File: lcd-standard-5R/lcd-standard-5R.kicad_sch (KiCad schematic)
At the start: 109 parts, among them J1 SWD, J2 Conn_01x40_MountingPin, J3 Micro_SD_Card_Det1, J5 Conn_01x06_MountingPin, J6 Serial, J7 Conn_ARM_JTAG_SWD_10, J8 Conn_01x02_MountingPin, J9 Conn_01x10_MountingPin, Q1 DMG2301L, Q2 MMBT3904, Q3 MMBT3904, Q4 MMBT3904, SW1 BOOT0, SW2 RST, U1 MAX98357A, U2 TPS61169, U3 XPT2046TS, U4 CAT24C256, U5 AMS1117-3.3, U6 siplex-som-s16

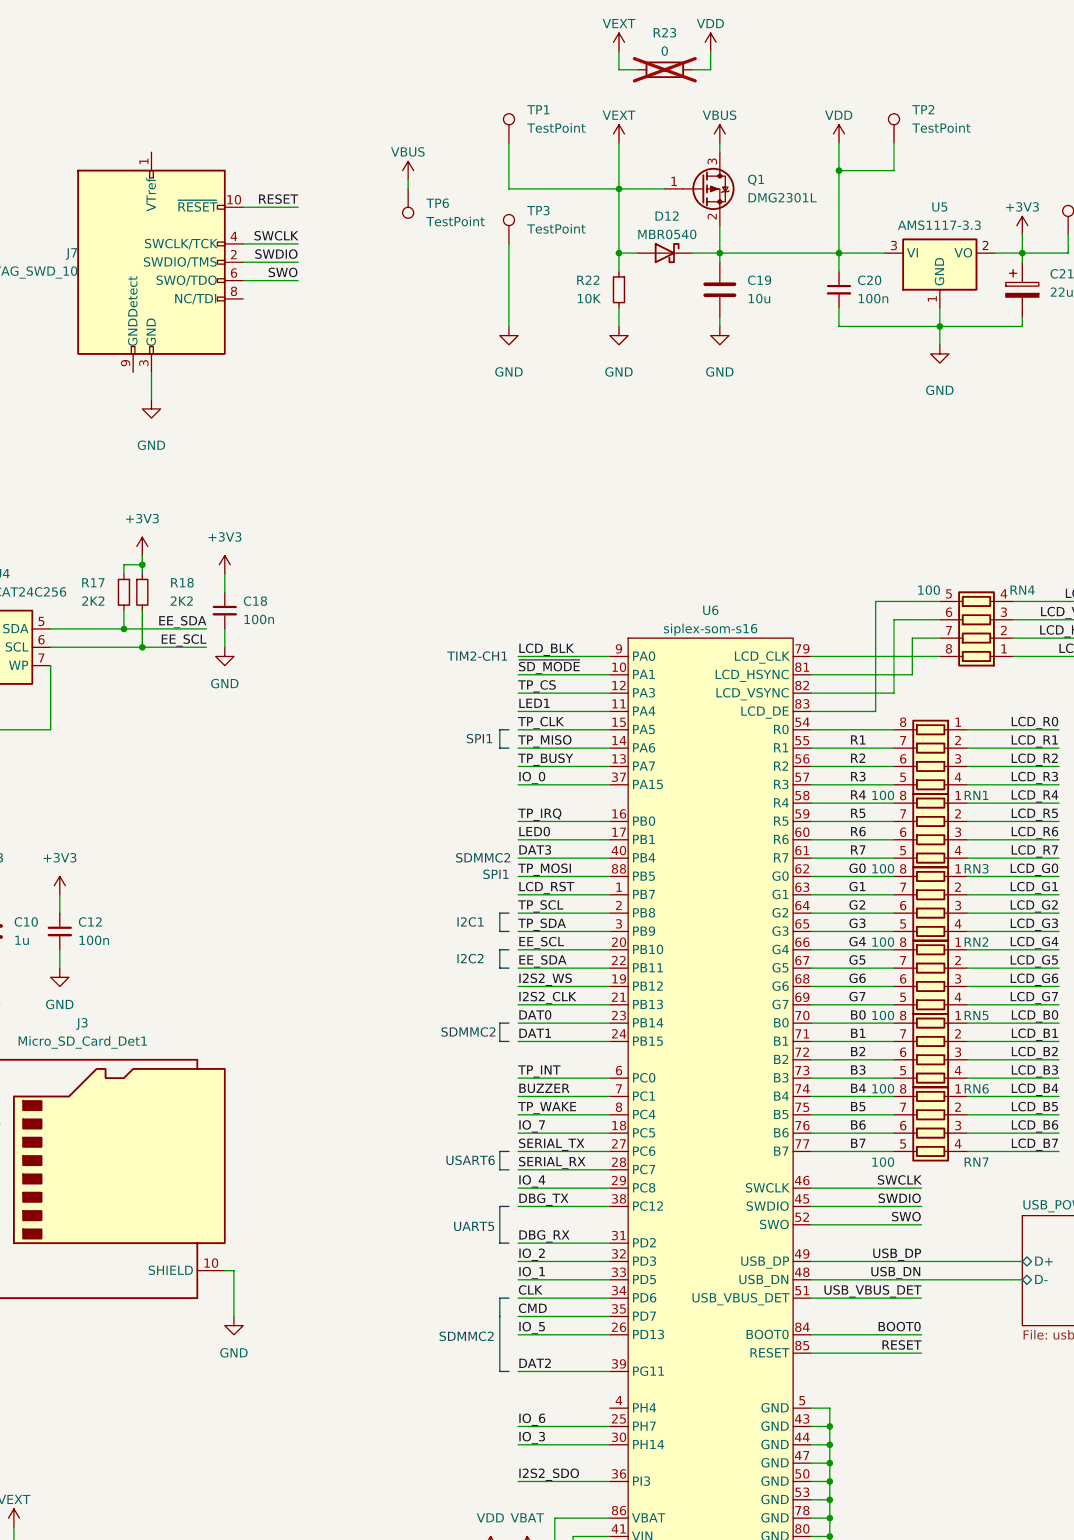
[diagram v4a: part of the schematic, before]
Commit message: Added sd_det tracks
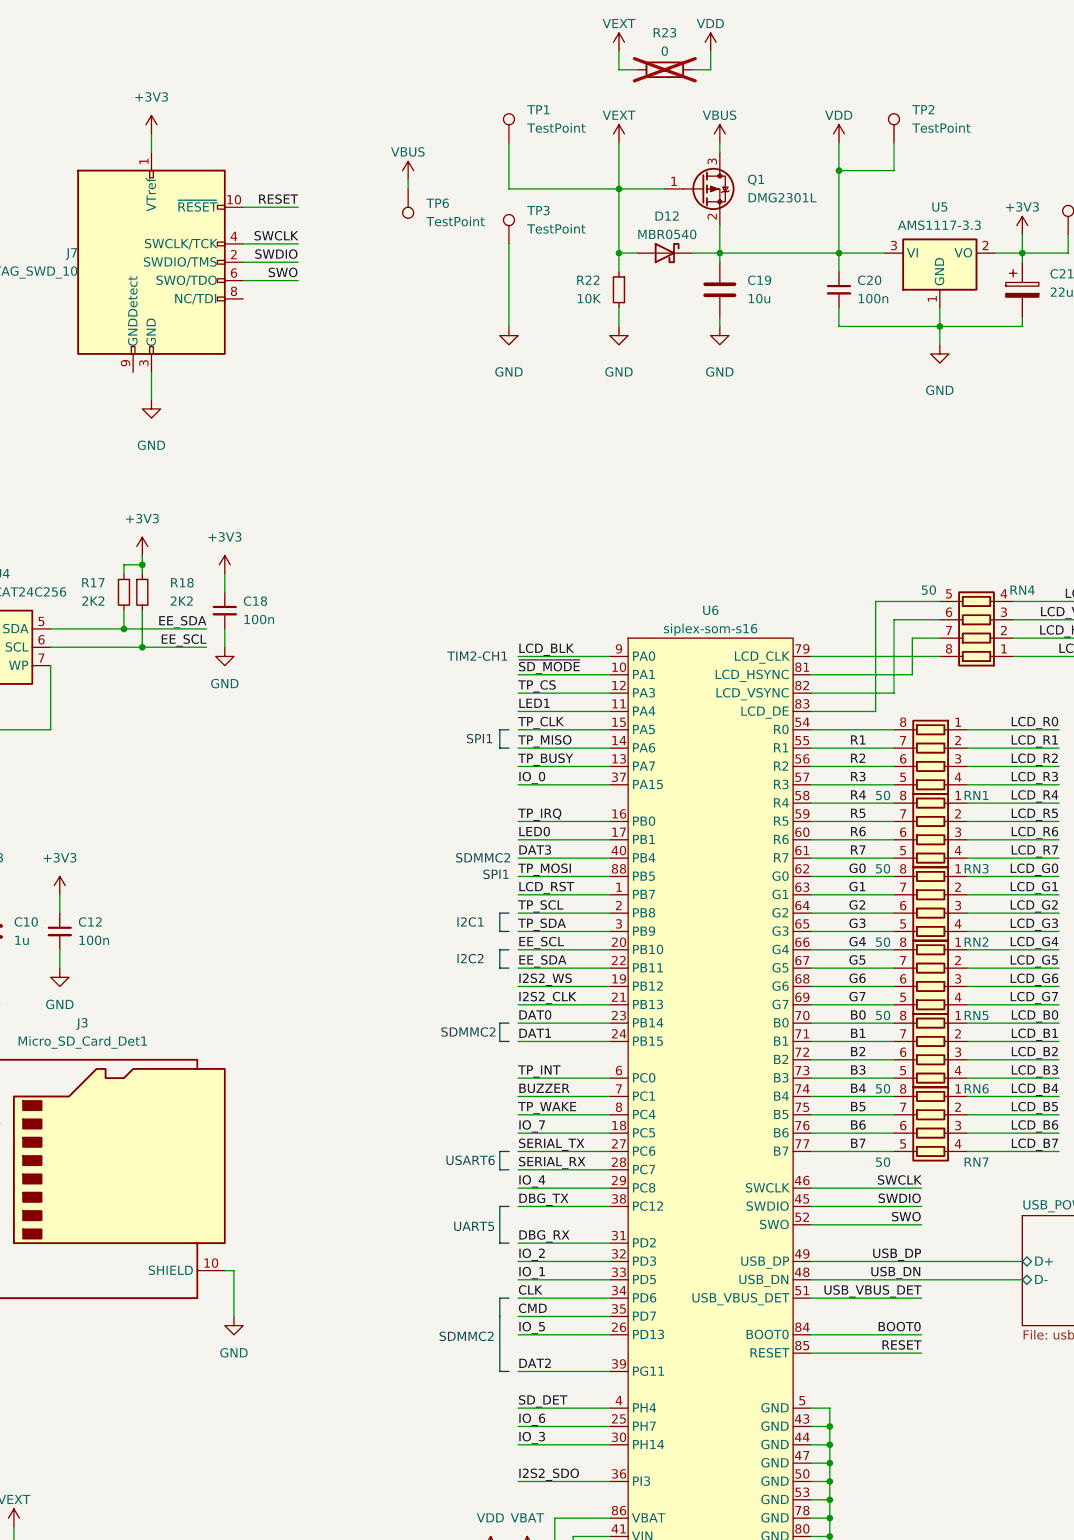
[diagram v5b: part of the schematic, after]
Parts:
- J5: footprint Connector_FFC-FPC:Hirose_FH12-6S-0.5SH_1x06-1MP_P0.50mm_Horizontal -> Connector_FPC:Conn_FPC_6P_0.5mm_XUNPU_FPC-05FB-6PH20
- J9: footprint Connector_JST:JST_SHL_SM10B-SHLS-TF_1x10-1MP_P1.00mm_Horizontal -> Connector_FPC:Conn_FPC_10P_1mm_G-SWITCH_GT-F1008SR20-10SMT01
- RN1, RN2, RN3, RN4, RN5, RN6, RN7: value 100 -> 50
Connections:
- net +3V3: now also J7.1 (VTref)
- net SD_DET: now also U6.4 (PH4)
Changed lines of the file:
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@@
 	(wire
 		(pts
+			(xy -26.67 -38.1) (xy -26.67 -35.56)
+		)
+		(stroke
+			(width 0)
+			(type default)
+		)
+	)
+	(wire
+		(pts
 			(xy 99.06 82.55) (xy 86.36 82.55)
 		)
@@
 	(wire
 		(pts
+			(xy 24.13 138.43) (xy 36.83 138.43)
+		)
+		(stroke
+			(width 0)
+			(type default)
+		)
+	)
+	(wire
+		(pts
 			(xy 238.76 64.77) (xy 251.46 64.77)
 		)
@@
 		)
 	)
+	(label "SD_DET"
+		(at 24.13 138.43 0)
+		(fields_autoplaced yes)
+		(effects
+			(font
+				(size 1.27 1.27)
+			)
+			(justify left bottom)
+		)
+	)
 	(label "SERIAL_TX"
 		(at 24.13 102.87 0)
@@
 			)
 		)
-		(property "Value" "100"
+		(property "Value" "50"
 			(at 74.676 53.594 90)
 			(effects
@@
 			)
 		)
-		(property "Value" "100"
+		(property "Value" "50"
 			(at 74.676 73.914 90)
 			(effects
@@
 			)
 		)
-		(property "Footprint" "Connector_FFC-FPC:Hirose_FH12-6S-0.5SH_1x06-1MP_P0.50mm_Horizontal"
+		(property "Footprint" "Connector_FPC:Conn_FPC_6P_0.5mm_XUNPU_FPC-05FB-6PH20"
 			(at 342.9 180.34 0)
 			(effects
@@
 	)
 	(symbol
+		(lib_id "power:+3V3")
+		(at -26.67 -38.1 0)
+		(unit 1)
+		(exclude_from_sim no)
+		(in_bom yes)
+		(on_board yes)
+		(dnp no)
+		(fields_autoplaced yes)
+		(property "Reference" "#PWR0107"
+			(at -26.67 -34.29 0)
+			(effects
+				(font
+					(size 1.27 1.27)
+				)
+				(hide yes)
+			)
+		)
+		(property "Value" "+3V3"
+			(at -26.67 -43.18 0)
+			(effects
+				(font
+					(size 1.27 1.27)
+				)
+			)
+		)
+		(property "Footprint" ""
+			(at -26.67 -38.1 0)
+			(effects
+				(font
+					(size 1.27 1.27)
+				)
+				(hide yes)
+			)
+		)
+		(property "Datasheet" ""
+			(at -26.67 -38.1 0)
+			(effects
+				(font
+					(size 1.27 1.27)
+				)
+				(hide yes)
+			)
+		)
+		(property "Description" "Power symbol creates a global label with name \"+3V3\""
+			(at -26.67 -38.1 0)
+			(effects
+				(font
+					(size 1.27 1.27)
+				)
+				(hide yes)
+			)
+		)
+		(pin "1"
+		)
+		(instances
+			(project "lcd-standard-5R"
+				(path "/a9fe5be7-3a80-455e-a721-d53819db4a52"
+					(reference "#PWR0107")
+					(unit 1)
+				)
+			)
+		)
+	)
+	(symbol
 		(lib_id "Device:C_Polarized")
 		(at 93.98 -16.51 0)
@@
 			)
 		)
-		(property "Value" "100"
+		(property "Value" "50"
 			(at 74.676 94.234 90)
 			(effects
@@
 			)
 		)
-		(property "Value" "100"
+		(property "Value" "50"
 			(at 74.676 104.394 90)
 			(effects
@@
 			)
 		)
-		(property "Value" "100"
+		(property "Value" "50"
 			(at 74.676 63.754 90)
 			(effects
@@
 			)
 		)
-		(property "Value" "100"
+		(property "Value" "50"
 			(at 74.676 84.074 90)
 			(effects
@@
 			)
 		)
-		(property "Footprint" "Connector_JST:JST_SHL_SM10B-SHLS-TF_1x10-1MP_P1.00mm_Horizontal"
+		(property "Footprint" "Connector_FPC:Conn_FPC_10P_1mm_G-SWITCH_GT-F1008SR20-10SMT01"
 			(at -107.95 49.53 0)
 			(effects
@@
 			)
 		)
-		(property "Value" "100"
+		(property "Value" "50"
 			(at 81.026 25.146 90)
 			(effects

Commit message: Slight changes
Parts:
- BT2: JLCPCB Part # (none) -> C70381
- BZ1: JLCPCB Part # (none) -> C255327
- C1: value 10u -> 10u/1206; JLCPCB Part # (none) -> C13585
- C10, C2, C22, C3: JLCPCB Part # (none) -> C15849
- C11, C19, C5, C7: JLCPCB Part # (none) -> C15850
- C12, C18: JLCPCB Part # (none) -> C1525
- C13, C14, C15, C16, C17, C20, C23, C4, C6: footprint Capacitor_SMD:C_0603_1608Metric -> Capacitor_SMD:C_0402_1005Metric; JLCPCB Part # (none) -> C1525
- C21: value 22uF -> 10uF; footprint Capacitor_Tantalum_SMD:CP_EIA-3528-12_Kemet-T -> Capacitor_Tantalum_SMD:CP_EIA-3216-18_Kemet-A; JLCPCB Part # (none) -> C7171
- D1: value NSR0320MW2T1G -> B5819WS; JLCPCB Part # (none) -> C64886
- D10, D11: JLCPCB Part # (none) -> C47546
- D12: value MBR0540 -> B5819W; JLCPCB Part # (none) -> C7420330
- D2: JLCPCB Part # (none) -> C7420330
- D3, D4: value LED -> RED; JLCPCB Part # (none) -> C84256
- D5: value LED -> GREEN; JLCPCB Part # (none) -> C2297
- D6, D7, D8, D9: JLCPCB Part # (none) -> C235771
- FB1: JLCPCB Part # (none) -> C1017
- J1: JLCPCB Part # (none) -> C5160763C5160763
- J2: JLCPCB Part # (none) -> C225713
- J3: JLCPCB Part # (none) -> C266621
- J5: JLCPCB Part # (none) -> C2856827
- J6: JLCPCB Part # (none) -> C146120
- J8: JLCPCB Part # (none) -> C7419891
- J9: JLCPCB Part # (none) -> C22387155
- L1: value 6.8u -> 4.7u; JLCPCB Part # (none) -> C57269
- Q1: value DMG2301L -> DMG3415; JLCPCB Part # (none) -> C7202986
- Q2, Q3, Q4: JLCPCB Part # (none) -> C7420353
- R1, R12, R13, R14, R15, R22, R25, R27, R29, R30, R31, R4, R7, R8: JLCPCB Part # (none) -> C25744
- R11, R16, R3: JLCPCB Part # (none) -> C4109
- R17, R18, R19, R20, R21, R5, R6: JLCPCB Part # (none) -> C25879
- R2: JLCPCB Part # (none) -> C23164
- R24, R26, R28: JLCPCB Part # (none) -> C11702
- R32: JLCPCB Part # (none) -> C25741
- R33: JLCPCB Part # (none) -> C26083
- RN1, RN2, RN3, RN4, RN5, RN6, RN7: JLCPCB Part # (none) -> C48442
- SW1, SW2: JLCPCB Part # (none) -> C127488
- TP1, TP2, TP3, TP4, TP5, TP6, TP7, U3, U6: now left out of the parts list
- U1: JLCPCB Part # (none) -> C910544
- U2: JLCPCB Part # (none) -> C71045
- U4: JLCPCB Part # (none) -> C6482
- U5: JLCPCB Part # (none) -> C6186

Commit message: Change LCD 5R to onboard MCU, cause separate boards are too expensive
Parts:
- removed BT2: S8411-45R, CR1220-Batt-conn-S8411-45R:CR1220-Batt-conn-S8411-45R, symbol CR1220-Batt-conn-S8411-45R:S8411-45R
- removed BZ1: MLT-9650, SMD-Buzzer:active-MLT-9650, symbol Device:Buzzer
- removed C1: 10u/1206, Capacitor_SMD:C_1206_3216Metric, symbol Device:C
- removed C10, C2, C22, C3: 1u, Capacitor_SMD:C_0603_1608Metric, symbol Device:C
- removed C11, C19, C5, C7: 10u, Capacitor_SMD:C_0805_2012Metric, symbol Device:C
- removed C12, C13, C14, C15, C16, C17, C18, C20, C6: 100n, Capacitor_SMD:C_0402_1005Metric, symbol Device:C_Small
- removed C21: 10uF, Capacitor_Tantalum_SMD:CP_EIA-3216-18_Kemet-A, symbol Device:C_Polarized
- removed C23, C4: 100n, Capacitor_SMD:C_0402_1005Metric, symbol Device:C
- removed D1: B5819WS, Diode_SMD:D_SOD-123, symbol Device:D
- removed D10, D11: BAT54S, Package_TO_SOT_SMD:SOT-23, symbol Diode:BAT54S
- removed D12: B5819W, Diode_SMD:D_SOD-123, symbol Diode:MBR0540
- removed D2: MBR0540, Diode_SMD:D_SOD-123, symbol Diode:MBR0540
- removed D3, D4: RED, LED_SMD:LED_0805_2012Metric, symbol Device:LED
- removed D5: GREEN, LED_SMD:LED_0805_2012Metric, symbol Device:LED
- removed D6, D7, D8, D9: MMSZ5226BT1G, Diode_SMD:D_SOD-123, symbol Device:D_Zener
- removed FB1: 600R/100MHz, Capacitor_SMD:C_0805_2012Metric, symbol Device:FerriteBead_Small
- removed J1: SWD, Connector_PinHeader_1.27mm:PinHeader_2x07_P1.27mm_Vertical_SMD, symbol Connector_Generic:Conn_02x07_Odd_Even
- removed J2: Conn_01x40_MountingPin, Connector_FFC-FPC:Omron_XF2M-4015-1A_1x40-1MP_P0.5mm_Horizontal, symbol Connector_Generic_MountingPin:Conn_01x40_MountingPin
- removed J3: Micro_SD_Card_Det1, TF-115:SD-TF-115, symbol Connector:Micro_SD_Card_Det1
- removed J5: Conn_01x06_MountingPin, Connector_FPC:Conn_FPC_6P_0.5mm_XUNPU_FPC-05FB-6PH20, symbol Connector_Generic_MountingPin:Conn_01x06_MountingPin
- removed J6: Serial, S4B-XH-SM4-TB_LF__SN:S4BXHSM4TBLFSN, symbol Connector_Generic_MountingPin:Conn_01x04_MountingPin
- removed J7: Conn_ARM_JTAG_SWD_10, Connector:Tag-Connect_TC2050-IDC-NL_2x05_P1.27mm_Vertical, symbol Connector:Conn_ARM_JTAG_SWD_10
- removed J8: Conn_01x02_MountingPin, Connector_Hirose:Hirose_DF13C_CL535-0402-2-51_1x02-1MP_P1.25mm_Vertical, symbol Connector_Generic_MountingPin:Conn_01x02_MountingPin
- removed J9: Conn_01x10_MountingPin, Connector_FPC:Conn_FPC_10P_1mm_G-SWITCH_GT-F1008SR20-10SMT01, symbol Connector_Generic_MountingPin:Conn_01x10_MountingPin
- removed JP1, JP2, JP3: JMP, Jumper:SolderJumper-2_P1.3mm_Open_RoundedPad1.0x1.5mm, symbol Jumper:SolderJumper_2_Open
- removed L1: 4.7u, Inductor_SMD:L_Abracon_ASPI-4030S, symbol Device:L_Small
- removed Q1: DMG3415, Package_TO_SOT_SMD:SOT-23, symbol Transistor_FET:DMG2301L
- removed Q2, Q3, Q4: MMBT3904, Package_TO_SOT_SMD:SOT-23, symbol Transistor_BJT:MMBT3904
- removed R1, R12, R13, R14, R15, R22, R25, R27, R29, R30, R31, R4, R7, R8: 10K, Resistor_SMD:R_0402_1005Metric, symbol Device:R_Small
- removed R11, R16, R3: 2K, Resistor_SMD:R_0402_1005Metric, symbol Device:R_Small
- removed R17, R18, R19, R20, R21, R5, R6: 2K2, Resistor_SMD:R_0402_1005Metric, symbol Device:R_Small
- removed R2: 4.7R, Resistor_SMD:R_0603_1608Metric, symbol Device:R_Small
- removed R23: 0, Resistor_SMD:R_1206_3216Metric, symbol Device:R
- removed R24, R26, R28: 1K, Resistor_SMD:R_0402_1005Metric, symbol Device:R_Small
- removed R32: 100K, Resistor_SMD:R_0402_1005Metric, symbol Device:R_Small
- removed R33: 1M, Resistor_SMD:R_0402_1005Metric, symbol Device:R_Small
- removed SW1: BOOT0, Button_Switch_SMD:SW_SPST_PTS810, symbol Switch:SW_Push
- removed SW2: RST, Button_Switch_SMD:SW_SPST_PTS810, symbol Switch:SW_Push
- removed TP1, TP2, TP3, TP4, TP5, TP6, TP7: TestPoint, TestPoint:TestPoint_Pad_D1.0mm, symbol Connector:TestPoint
- removed U1: MAX98357A, Package_DFN_QFN:TQFN-16-1EP_3x3mm_P0.5mm_EP1.23x1.23mm, symbol Audio:MAX98357A
- removed U2: TPS61169, Package_TO_SOT_SMD:SOT-23-5, symbol Regulator_Switching:TPS61040DBV
- removed U3: XPT2046TS, Package_SO:TSSOP-16_4.4x5mm_P0.65mm, symbol Driver_Display:XPT2046TS
- removed U4: CAT24C256, Package_SO:SOIC-8_3.9x4.9mm_P1.27mm, symbol Memory_EEPROM:CAT24C256
- removed U5: AMS1117-3.3, Package_TO_SOT_SMD:SOT-223-3_TabPin2, symbol Regulator_Linear:AMS1117-3.3
- renumbered RN3 to RN2, RN2 to RN3, RN5 to RN4, RN6 to RN5, RN7 to RN6, RN4 to RN7, U6 to U1
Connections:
- no-connect marks 7 -> 1
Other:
- added sheet DISPLAY (lcd_display_40p.kicad_sch)
- added sheet IO (input-output.kicad_sch)
- added sheet MCU (STM32H743ZITx.kicad_sch)
- added sheet MEMORY_EEPROM (24C256.kicad_sch)
- added sheet MEMORY_FLASH (W25Q512.kicad_sch)
- added sheet MEMORY_FMC (SDRAM.kicad_sch)
- added sheet MEMORY_SD_CARD (uSD_Card.kicad_sch)
- added sheet OUTPUT_SPEAKER (MAX98357.kicad_sch)
- note removed: "45mA"
